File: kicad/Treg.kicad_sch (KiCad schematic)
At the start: 31 parts, among them U1 PMW3360, U2 TPS73601DBV, U4 XIAO-ESP32-S3-DIP

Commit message: adjust layout
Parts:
- renumbered U4 to U3
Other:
- moved on the sheet: C1, C11, C12, C13, C14, C2, C21, C22, C23, C24, C25, C26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

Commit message: add python
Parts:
- added J1, J2, J3, J4, J5, J6: Conn_01x02, Connector_PinHeader_2.54mm:PinHeader_1x02_P2.54mm_Vertical, symbol Connector_Generic:Conn_01x02
- added J7, J8: Conn_01x07, Connector_PinHeader_2.54mm:PinHeader_1x07_P2.54mm_Vertical, symbol Connector_Generic:Conn_01x07
- C1, C11, C12, C13, C14, C2, C21, C22, C23, C24, C25, C26: footprint (none) -> Capacitor_SMD:C_0603_1608Metric_Pad1.08x0.95mm_HandSolder
- R1, R11, R12, R13, R14, R15, R16, R17, R18, R19, R2, R20, R21, R22, R3, R4: footprint (none) -> Resistor_SMD:R_0603_1608Metric_Pad0.98x0.95mm_HandSolder
- U1: footprint (none) -> PMW3360:PMW3360
- U2: footprint Package_TO_SOT_SMD:SOT-23-5 -> Package_TO_SOT_SMD:TSOT-23-5_HandSoldering
- U3: footprint Module:MOUDLE14P-XIAO-DIP-SMD -> RF_Module:MCU_Seeed_ESP32C3
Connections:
- net 3V3: now also J8.3 (Pin_3)
- net DSW1: now also J7.1 (Pin_1)
- net DSW2: now also J7.2 (Pin_2)
- net DSW3: now also J7.3 (Pin_3)
- net DSW4: now also J7.4 (Pin_4)
- net DSW5: now also J7.5 (Pin_5)
- net DSW6: now also J7.6 (Pin_6)
- net GND: now also J1.2 (Pin_2), J2.2 (Pin_2), J3.2 (Pin_2), J4.2 (Pin_2), J5.2 (Pin_2), J6.2 (Pin_2), J8.2 (Pin_2)
- net MISO: now also J8.5 (Pin_5)
- net MOSI: now also J8.4 (Pin_4)
- net NCS: now also J8.7 (Pin_7)
- net SCLK: now also J8.6 (Pin_6)
- net SW1: now also J1.1 (Pin_1)
- net SW2: now also J2.1 (Pin_1)
- net SW3: now also J3.1 (Pin_1)
- net SW4: now also J4.1 (Pin_1)
- net SW5: now also J5.1 (Pin_1)
- net SW6: now also J6.1 (Pin_1)
- net VBUS: now also J8.1 (Pin_1)
- no-connect marks 1 -> 2
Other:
- moved on the sheet: C24, C25, C26, R17, R18, R19, R20, R21, R22

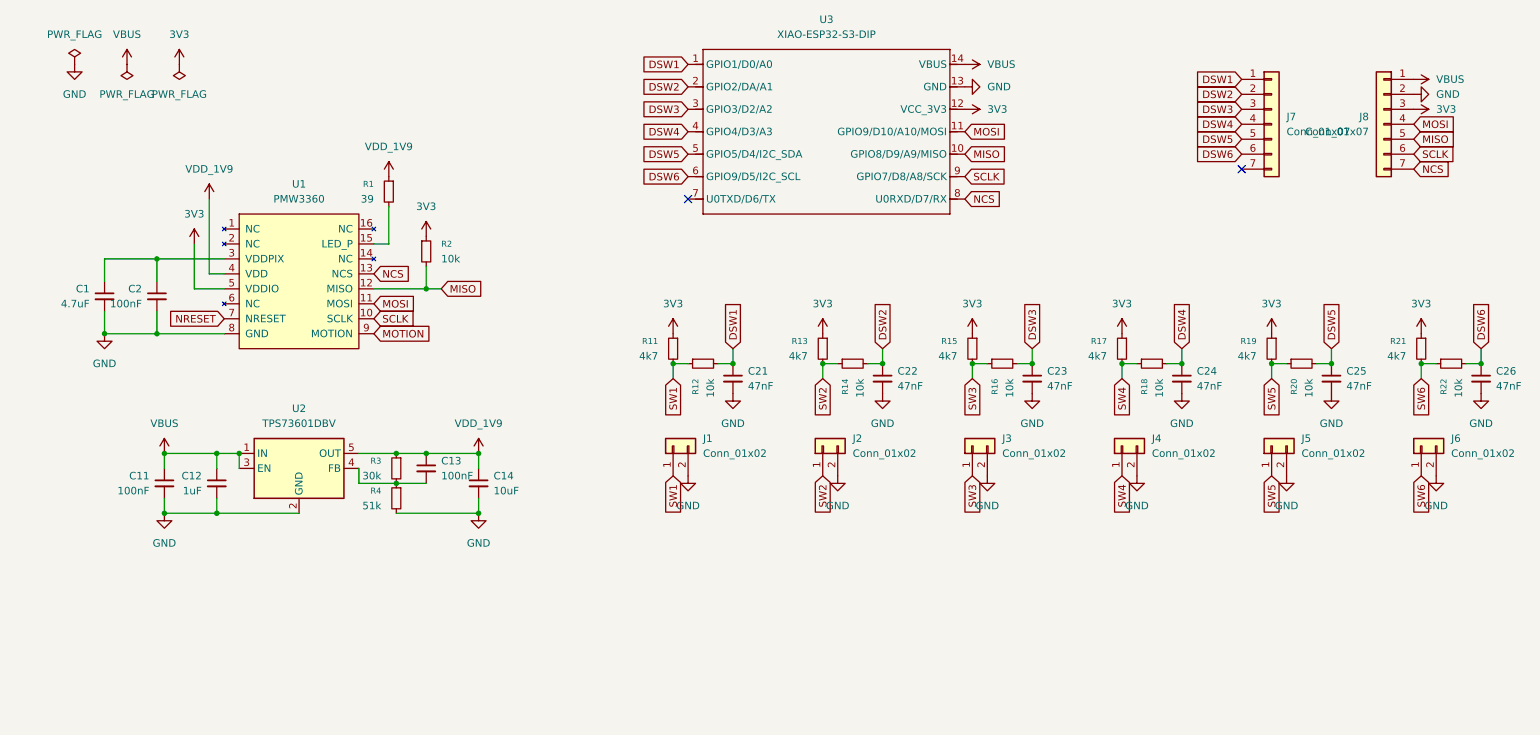
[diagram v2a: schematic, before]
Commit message: add footprints, bat
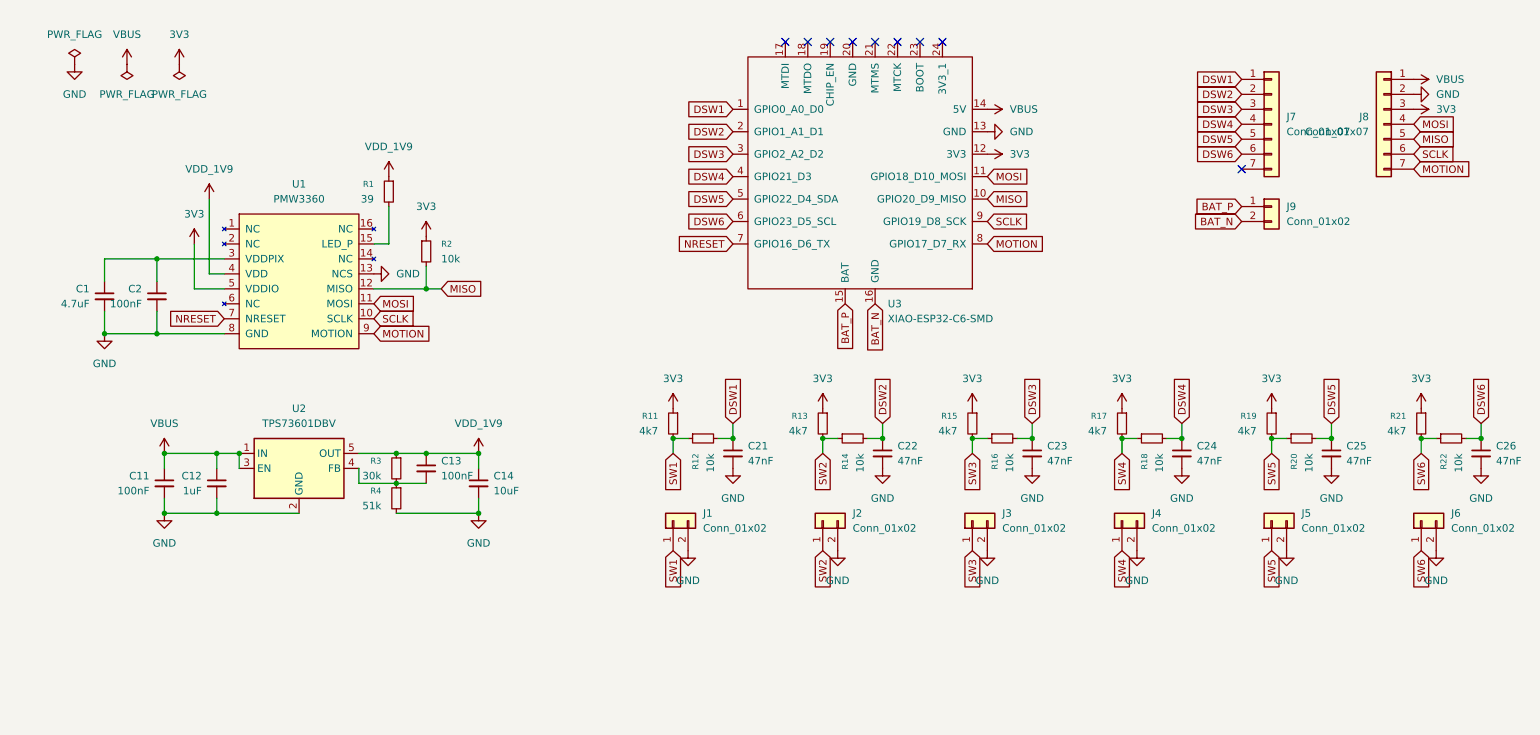
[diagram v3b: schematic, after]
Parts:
- removed U3: XIAO-ESP32-S3-DIP, RF_Module:MCU_Seeed_ESP32C3, symbol Seeed_Studio_XIAO_Series:XIAO-ESP32-S3-DIP
- added J9: Conn_01x02, Connector_PinHeader_2.54mm:PinHeader_1x02_P2.54mm_Vertical, symbol Connector_Generic:Conn_01x02
- added U3: XIAO-ESP32-C6-SMD, footprint:BatJumper, symbol Seeed_Studio_XIAO_Series:XIAO-ESP32-C6-SMD
- U1: footprint PMW3360:PMW3360 -> footprint:PMW3360
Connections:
- net 3V3: now also U3.12 (3V3)
- net DSW1: now also U3.1 (GPIO0_A0_D0)
- net DSW2: now also U3.2 (GPIO1_A1_D1)
- net DSW3: now also U3.3 (GPIO2_A2_D2)
- net DSW4: now also U3.4 (GPIO21_D3)
- net DSW5: now also U3.5 (GPIO22_D4_SDA)
- net DSW6: now also U3.6 (GPIO23_D5_SCL)
- net GND: now also U1.13 (NCS), U3.13 (GND)
- net MISO: now also U3.10 (GPIO20_D9_MISO)
- net MOSI: now also U3.11 (GPIO18_D10_MOSI)
- net MOTION: now also J8.7 (Pin_7), U3.8 (GPIO17_D7_RX)
- net NRESET: now also U3.7 (GPIO16_D6_TX)
- net SCLK: now also U3.9 (GPIO19_D8_SCK)
- net VBUS: now also U3.14 (5V)
- removed net NCS: J8.7 (Pin_7), U1.13 (NCS)
- new net BAT_N: J9.2 (Pin_2), U3.16 (GND)
- new net BAT_P: J9.1 (Pin_1), U3.15 (BAT)
- no-connect marks 2 -> 9
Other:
- moved on the sheet: C21, C22, C23, C24, C25, C26, J1, J2, J3, J4, J5, J6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

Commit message: place mods
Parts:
- removed C26: 47nF, Capacitor_SMD:C_0603_1608Metric_Pad1.08x0.95mm_HandSolder, symbol Device:C_Small
- removed J6: Conn_01x02, Connector_PinHeader_2.54mm:PinHeader_1x02_P2.54mm_Vertical, symbol Connector_Generic:Conn_01x02
- removed R21: 4k7, Resistor_SMD:R_0603_1608Metric_Pad0.98x0.95mm_HandSolder, symbol Device:R_Small
- removed R22: 10k, Resistor_SMD:R_0603_1608Metric_Pad0.98x0.95mm_HandSolder, symbol Device:R_Small
- added C3, C4, C5, C6: 100nF, Capacitor_SMD:C_0603_1608Metric_Pad1.08x0.95mm_HandSolder, symbol Device:C_Small
- added H1, H2, H3, H4: MountingHole, MountingHole:MountingHole_2.2mm_M2, symbol Mechanical:MountingHole
- J9: footprint Connector_PinHeader_2.54mm:PinHeader_1x02_P2.54mm_Vertical -> footprint:BatJumper
- U3: footprint footprint:BatJumper -> Seeed Studio XIAO Series Library:XIAO-ESP32C6-SMD
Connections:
- net 3V3: now also C3.1, C4.1
- net GND: now also C3.2, C4.2, C5.2, C6.2; no longer U1.13 (NCS)
- net NRESET: now also J7.7 (Pin_7)
- net VDD_1V9: now also C5.1, C6.1
- net DSW6 renamed NCS
- net NCS: now also U1.13 (NCS)
- no-connect marks 9 -> 8

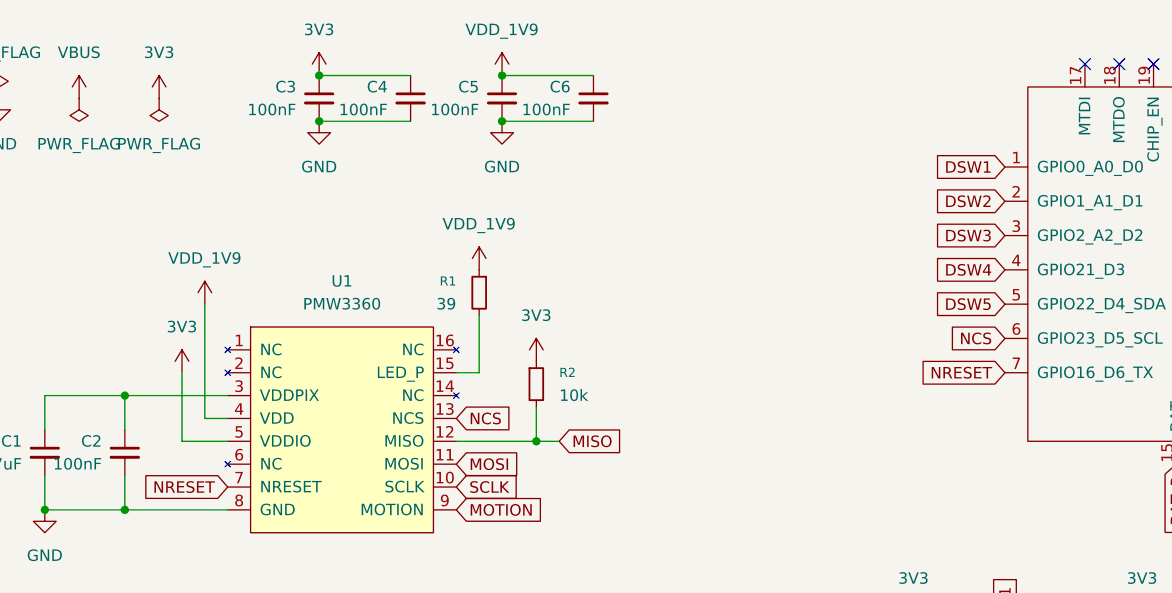
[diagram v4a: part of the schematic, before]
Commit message: replace parts with non-hand-solder, adjust refs
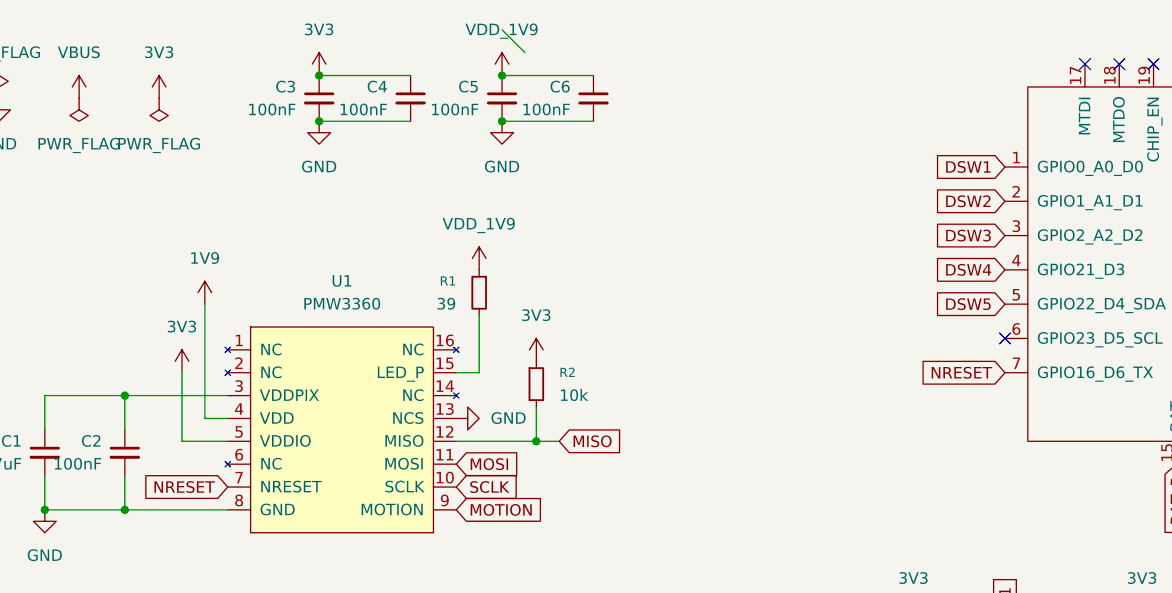
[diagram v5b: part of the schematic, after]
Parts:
- C1, C11, C12, C13, C14, C2, C21, C22, C23, C24, C25, C3, C4, C5, C6: footprint Capacitor_SMD:C_0603_1608Metric_Pad1.08x0.95mm_HandSolder -> Capacitor_SMD:C_0603_1608Metric
- R1, R11, R12, R13, R14, R15, R16, R17, R18, R19, R2, R20, R3, R4: footprint Resistor_SMD:R_0603_1608Metric_Pad0.98x0.95mm_HandSolder -> Resistor_SMD:R_0603_1608Metric
- U2: footprint Package_TO_SOT_SMD:TSOT-23-5_HandSoldering -> Package_TO_SOT_SMD:TSOT-23-5
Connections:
- net GND: now also U1.13 (NCS)
- net NCS: no longer U1.13 (NCS), U3.6 (GPIO23_D5_SCL)
- net VDD_1V9: no longer U1.4 (VDD)
- new net 1V9: U1.4 (VDD)
- no-connect marks 8 -> 9
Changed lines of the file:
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@@
 	)
 	(no_connect
+		(at 137.16 52.07)
+	)
+	(no_connect
 		(at 165.1 21.59)
 	)
+	(bus_entry
+		(at 81.28 17.78)
+		(size 2.54 2.54)
+		(stroke
+			(width 0)
+			(type default)
+		)
+	)
 	(wire
 		(pts
@@
 		)
 	)
-	(global_label "NCS"
-		(shape input)
-		(at 137.16 52.07 180)
-		(fields_autoplaced yes)
-		(effects
-			(font
-				(size 1.27 1.27)
-			)
-			(justify right)
-		)
-		(property "Intersheetrefs" "${INTERSHEET_REFS}"
-			(at 130.3648 52.07 0)
-			(effects
-				(font
-					(size 1.27 1.27)
-				)
-				(justify right)
-				(hide yes)
-			)
-		)
-	)
 	(global_label "SW3"
 		(shape input)
@@
 		)
 	)
-	(global_label "NCS"
-		(shape input)
-		(at 76.2 60.96 0)
-		(fields_autoplaced yes)
-		(effects
-			(font
-				(size 1.27 1.27)
-			)
-			(justify left)
-		)
-		(property "Intersheetrefs" "${INTERSHEET_REFS}"
-			(at 82.9952 60.96 0)
-			(effects
-				(font
-					(size 1.27 1.27)
-				)
-				(justify left)
-				(hide yes)
-			)
-		)
-	)
 	(symbol
 		(lib_id "Device:R_Small")
@@
 			)
 		)
-		(property "Footprint" "Resistor_SMD:R_0603_1608Metric_Pad0.98x0.95mm_HandSolder"
+		(property "Footprint" "Resistor_SMD:R_0603_1608Metric"
 			(at 157.48 88.9 0)
 			(effects
@@
 			)
 		)
-		(property "Footprint" "Resistor_SMD:R_0603_1608Metric_Pad0.98x0.95mm_HandSolder"
+		(property "Footprint" "Resistor_SMD:R_0603_1608Metric"
 			(at 182.88 88.9 0)
 			(effects
@@
 			)
 		)
-		(property "Footprint" "Resistor_SMD:R_0603_1608Metric_Pad0.98x0.95mm_HandSolder"
+		(property "Footprint" "Resistor_SMD:R_0603_1608Metric"
 			(at 177.8 86.36 0)
 			(effects
@@
 			)
 		)
-		(property "Footprint" "Capacitor_SMD:C_0603_1608Metric_Pad1.08x0.95mm_HandSolder"
+		(property "Footprint" "Capacitor_SMD:C_0603_1608Metric"
 			(at 30.48 64.77 0)
 			(effects
@@
 			)
 		)
-		(property "Footprint" "Resistor_SMD:R_0603_1608Metric_Pad0.98x0.95mm_HandSolder"
+		(property "Footprint" "Resistor_SMD:R_0603_1608Metric"
 			(at 152.4 86.36 0)
 			(effects
@@
 			)
 		)
-		(property "Footprint" "Resistor_SMD:R_0603_1608Metric_Pad0.98x0.95mm_HandSolder"
+		(property "Footprint" "Resistor_SMD:R_0603_1608Metric"
 			(at 78.74 46.99 0)
 			(effects
@@
 			)
 		)
-		(property "Footprint" "Package_TO_SOT_SMD:TSOT-23-5_HandSoldering"
+		(property "Footprint" "Package_TO_SOT_SMD:TSOT-23-5"
 			(at 63.5 85.725 0)
 			(effects
@@
 			)
 		)
-		(property "Footprint" "Capacitor_SMD:C_0603_1608Metric_Pad1.08x0.95mm_HandSolder"
+		(property "Footprint" "Capacitor_SMD:C_0603_1608Metric"
 			(at 91.44 25.4 0)
 			(effects
@@
 			)
 		)
-		(property "Footprint" "Resistor_SMD:R_0603_1608Metric_Pad0.98x0.95mm_HandSolder"
+		(property "Footprint" "Resistor_SMD:R_0603_1608Metric"
 			(at 233.68 88.9 0)
 			(effects
@@
 			)
 		)
-		(property "Footprint" "Resistor_SMD:R_0603_1608Metric_Pad0.98x0.95mm_HandSolder"
+		(property "Footprint" "Resistor_SMD:R_0603_1608Metric"
 			(at 132.08 88.9 0)
 			(effects
@@
 			)
 		)
-		(property "Footprint" "Resistor_SMD:R_0603_1608Metric_Pad0.98x0.95mm_HandSolder"
+		(property "Footprint" "Resistor_SMD:R_0603_1608Metric"
 			(at 127 86.36 0)
 			(effects
@@
 	)
 	(symbol
+		(lib_id "power:GND")
+		(at 76.2 60.96 90)
+		(unit 1)
+		(exclude_from_sim no)
+		(in_bom yes)
+		(on_board yes)
+		(dnp no)
+		(fields_autoplaced yes)
+		(property "Reference" "#PWR034"
+			(at 82.55 60.96 0)
+			(effects
+				(font
+					(size 1.27 1.27)
+				)
+				(hide yes)
+			)
+		)
+		(property "Value" "GND"
+			(at 80.01 60.9599 90)
+			(effects
+				(font
+					(size 1.27 1.27)
+				)
+				(justify right)
+			)
+		)
+		(property "Footprint" ""
+			(at 76.2 60.96 0)
+			(effects
+				(font
+					(size 1.27 1.27)
+				)
+				(hide yes)
+			)
+		)
+		(property "Datasheet" ""
+			(at 76.2 60.96 0)
+			(effects
+				(font
+					(size 1.27 1.27)
+				)
+				(hide yes)
+			)
+		)
+		(property "Description" "Power symbol creates a global label with name \"GND\" , ground"
+			(at 76.2 60.96 0)
+			(effects
+				(font
+					(size 1.27 1.27)
+				)
+				(hide yes)
+			)
+		)
+		(pin "1"
+		)
+		(instances
+			(project "Treg"
+				(path "/cc713380-d5d4-4611-b364-320b19da6c16"
+					(reference "#PWR034")
+					(unit 1)
+				)
+			)
+		)
+	)
+	(symbol
 		(lib_id "power:PWR_FLAG")
 		(at 43.18 25.4 180)
@@
 			)
 		)
-		(property "Footprint" "Resistor_SMD:R_0603_1608Metric_Pad0.98x0.95mm_HandSolder"
+		(property "Footprint" "Resistor_SMD:R_0603_1608Metric"
 			(at 80.01 99.06 0)
 			(effects
@@
 			)
 		)
-		(property "Footprint" "Capacitor_SMD:C_0603_1608Metric_Pad1.08x0.95mm_HandSolder"
+		(property "Footprint" "Capacitor_SMD:C_0603_1608Metric"
 			(at 81.28 25.4 0)
 			(effects
@@
 			)
 		)
-		(property "Footprint" "Capacitor_SMD:C_0603_1608Metric_Pad1.08x0.95mm_HandSolder"
+		(property "Footprint" "Capacitor_SMD:C_0603_1608Metric"
 			(at 85.09 93.98 0)
 			(effects
@@
 			)
 		)
-		(property "Footprint" "Capacitor_SMD:C_0603_1608Metric_Pad1.08x0.95mm_HandSolder"
+		(property "Footprint" "Capacitor_SMD:C_0603_1608Metric"
 			(at 60.96 25.4 0)
 			(effects
@@
 			)
 		)
-		(property "Footprint" "Resistor_SMD:R_0603_1608Metric_Pad0.98x0.95mm_HandSolder"
+		(property "Footprint" "Resistor_SMD:R_0603_1608Metric"
 			(at 85.09 57.15 0)
 			(effects
@@
 			)
 		)
-		(property "Footprint" "Resistor_SMD:R_0603_1608Metric_Pad0.98x0.95mm_HandSolder"
+		(property "Footprint" "Resistor_SMD:R_0603_1608Metric"
 			(at 203.2 86.36 0)
 			(effects
@@
 			)
 		)
-		(property "Footprint" "Capacitor_SMD:C_0603_1608Metric_Pad1.08x0.95mm_HandSolder"
+		(property "Footprint" "Capacitor_SMD:C_0603_1608Metric"
 			(at 238.76 91.44 0)
 			(effects
@@
 			)
 		)
-		(property "Footprint" "Capacitor_SMD:C_0603_1608Metric_Pad1.08x0.95mm_HandSolder"
+		(property "Footprint" "Capacitor_SMD:C_0603_1608Metric"
 			(at 39.37 64.77 0)
 			(effects
@@
 			)
 		)
-		(property "Footprint" "Capacitor_SMD:C_0603_1608Metric_Pad1.08x0.95mm_HandSolder"
+		(property "Footprint" "Capacitor_SMD:C_0603_1608Metric"
 			(at 40.64 96.52 0)
 			(effects
@@
 			)
 		)
-		(property "Footprint" "Capacitor_SMD:C_0603_1608Metric_Pad1.08x0.95mm_HandSolder"
+		(property "Footprint" "Capacitor_SMD:C_0603_1608Metric"
 			(at 49.53 96.52 0)
 			(effects
@@
 			)
 		)
-		(property "Footprint" "Resistor_SMD:R_0603_1608Metric_Pad0.98x0.95mm_HandSolder"
+		(property "Footprint" "Resistor_SMD:R_0603_1608Metric"
 			(at 80.01 93.98 0)
 			(effects
@@
 			)
 		)
-		(property "Footprint" "Resistor_SMD:R_0603_1608Metric_Pad0.98x0.95mm_HandSolder"
+		(property "Footprint" "Resistor_SMD:R_0603_1608Metric"
 			(at 228.6 86.36 0)
 			(effects
@@
 			)
 		)
-		(property "Footprint" "Capacitor_SMD:C_0603_1608Metric_Pad1.08x0.95mm_HandSolder"
+		(property "Footprint" "Capacitor_SMD:C_0603_1608Metric"
 			(at 93.98 96.52 0)
 			(effects
@@
 			)
 		)
-		(property "Footprint" "Capacitor_SMD:C_0603_1608Metric_Pad1.08x0.95mm_HandSolder"
+		(property "Footprint" "Capacitor_SMD:C_0603_1608Metric"
 			(at 213.36 91.44 0)
 			(effects
@@
 			)
 		)
-		(property "Footprint" "Resistor_SMD:R_0603_1608Metric_Pad0.98x0.95mm_HandSolder"
+		(property "Footprint" "Resistor_SMD:R_0603_1608Metric"
 			(at 208.28 88.9 0)
 			(effects
@@
 			)
 		)
-		(property "Value" "VDD_1V9"
+		(property "Value" "1V9"
 			(at 48.26 43.18 0)
 			(effects
@@
 			)
 		)
-		(property "Footprint" "Capacitor_SMD:C_0603_1608Metric_Pad1.08x0.95mm_HandSolder"
+		(property "Footprint" "Capacitor_SMD:C_0603_1608Metric"
 			(at 187.96 91.44 0)
 			(effects
@@
 			)
 		)
-		(property "Footprint" "Capacitor_SMD:C_0603_1608Metric_Pad1.08x0.95mm_HandSolder"
+		(property "Footprint" "Capacitor_SMD:C_0603_1608Metric"
 			(at 162.56 91.44 0)
 			(effects
@@
 			)
 		)
-		(property "Footprint" "Capacitor_SMD:C_0603_1608Metric_Pad1.08x0.95mm_HandSolder"
+		(property "Footprint" "Capacitor_SMD:C_0603_1608Metric"
 			(at 137.16 91.44 0)
 			(effects
@@
 			)
 		)
-		(property "Footprint" "Capacitor_SMD:C_0603_1608Metric_Pad1.08x0.95mm_HandSolder"
+		(property "Footprint" "Capacitor_SMD:C_0603_1608Metric"
 			(at 71.12 25.4 0)
 			(effects

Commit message: wire sw, ldo
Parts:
- R1: footprint Resistor_SMD:R_0603_1608Metric -> Resistor_SMD:R_0603_1608Metric_Pad0.98x0.95mm_HandSolder
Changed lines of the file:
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@@
 			)
 		)
-		(property "Footprint" "Resistor_SMD:R_0603_1608Metric"
+		(property "Footprint" "Resistor_SMD:R_0603_1608Metric_Pad0.98x0.95mm_HandSolder"
 			(at 78.74 46.99 0)
 			(effects

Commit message: wiring gnd
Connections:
- net NCS is gone; now on net DSW5: J7.6 (Pin_6)
- net DSW1: now also J7.2 (Pin_2), U3.2 (GPIO1_A1_D1); no longer J7.1 (Pin_1), U3.1 (GPIO0_A0_D0)
- net DSW2: now also J7.3 (Pin_3), U3.3 (GPIO2_A2_D2); no longer J7.2 (Pin_2), U3.2 (GPIO1_A1_D1)
- net DSW3: now also J7.4 (Pin_4), U3.4 (GPIO21_D3); no longer J7.3 (Pin_3), U3.3 (GPIO2_A2_D2)
- net DSW4: now also J7.5 (Pin_5), U3.5 (GPIO22_D4_SDA); no longer J7.4 (Pin_4), U3.4 (GPIO21_D3)
- net DSW5: now also U3.6 (GPIO23_D5_SCL); no longer J7.5 (Pin_5), U3.5 (GPIO22_D4_SDA)
- no-connect marks 9 -> 10
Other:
- moved on the sheet: C21, C22, C23, C24, C25, J1, J2, J3, J4, J5, J7, J8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

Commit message: wiring almost done
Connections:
- net VDD_1V9 is gone; now on net 1V9: C13.1, C14.1, C5.1, C6.1, R1.1, R3.1, U2.5 (OUT)
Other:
- moved on the sheet: C3, C4, C5, C6
